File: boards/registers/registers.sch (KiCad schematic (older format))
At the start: 0 parts

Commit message: General-purpose register
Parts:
- added D? (x8): LED, symbol Device:LED
- added R? (x8): LED, symbol Device:R
- added R? (x8): 10k, symbol Device:R
- added U?: 74AC273, symbol 74xx:74HCT273
- added U?: 74ACT244, symbol 74xx:74HC244
- added U? (x3): 74LS08, symbol 74xx:74LS08
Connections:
- net labels added: GND, VCC, a[0..15], a_we, alu_a[0..7], alu_b0, alu_b1, alu_b2, alu_b3, alu_b4, alu_b5, alu_b6, alu_b7, alu_b[0..7], b_we, clk, d0, d1, d2, d3, d4, d5, d6, d7, d[0..7], di0, di1, di2, di3, di4, di5, di6, di7, di[0..7], ir_out0, ir_out1, ir_out2, ir_out3, ir_out4, ir_out5, ir_out6, ir_out7, ir_out[0..7], ir_we, oe_a_d, oe_b_alu, oe_b_d, ~clk, ~d_to_di_oe, ~rst
- wire segments 0 -> 76
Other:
- note added: "5 mA each"
- note added: "IR"
- note added: "TODO\nremove extra chip"

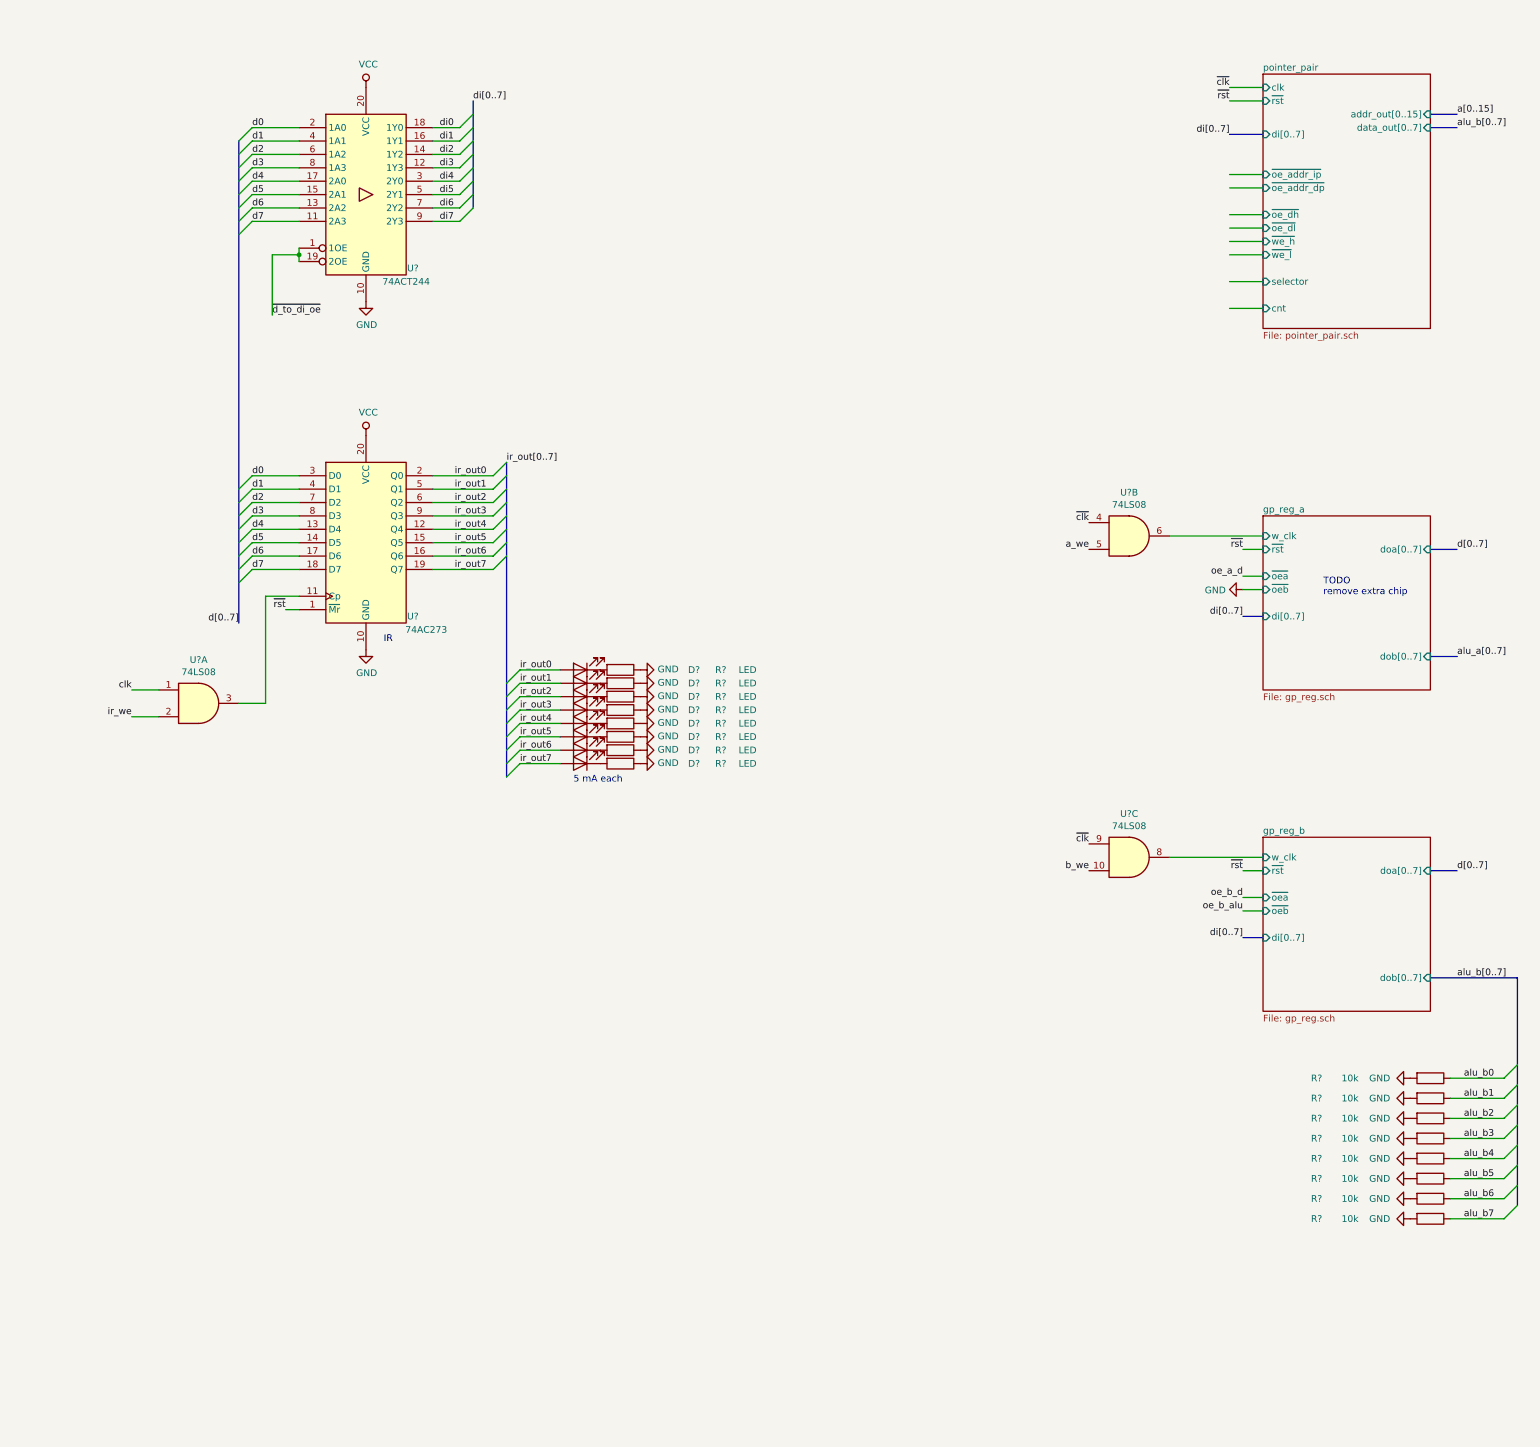
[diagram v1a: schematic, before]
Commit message: Rename some signals in CPU, add capacitors and signal names to the schematics
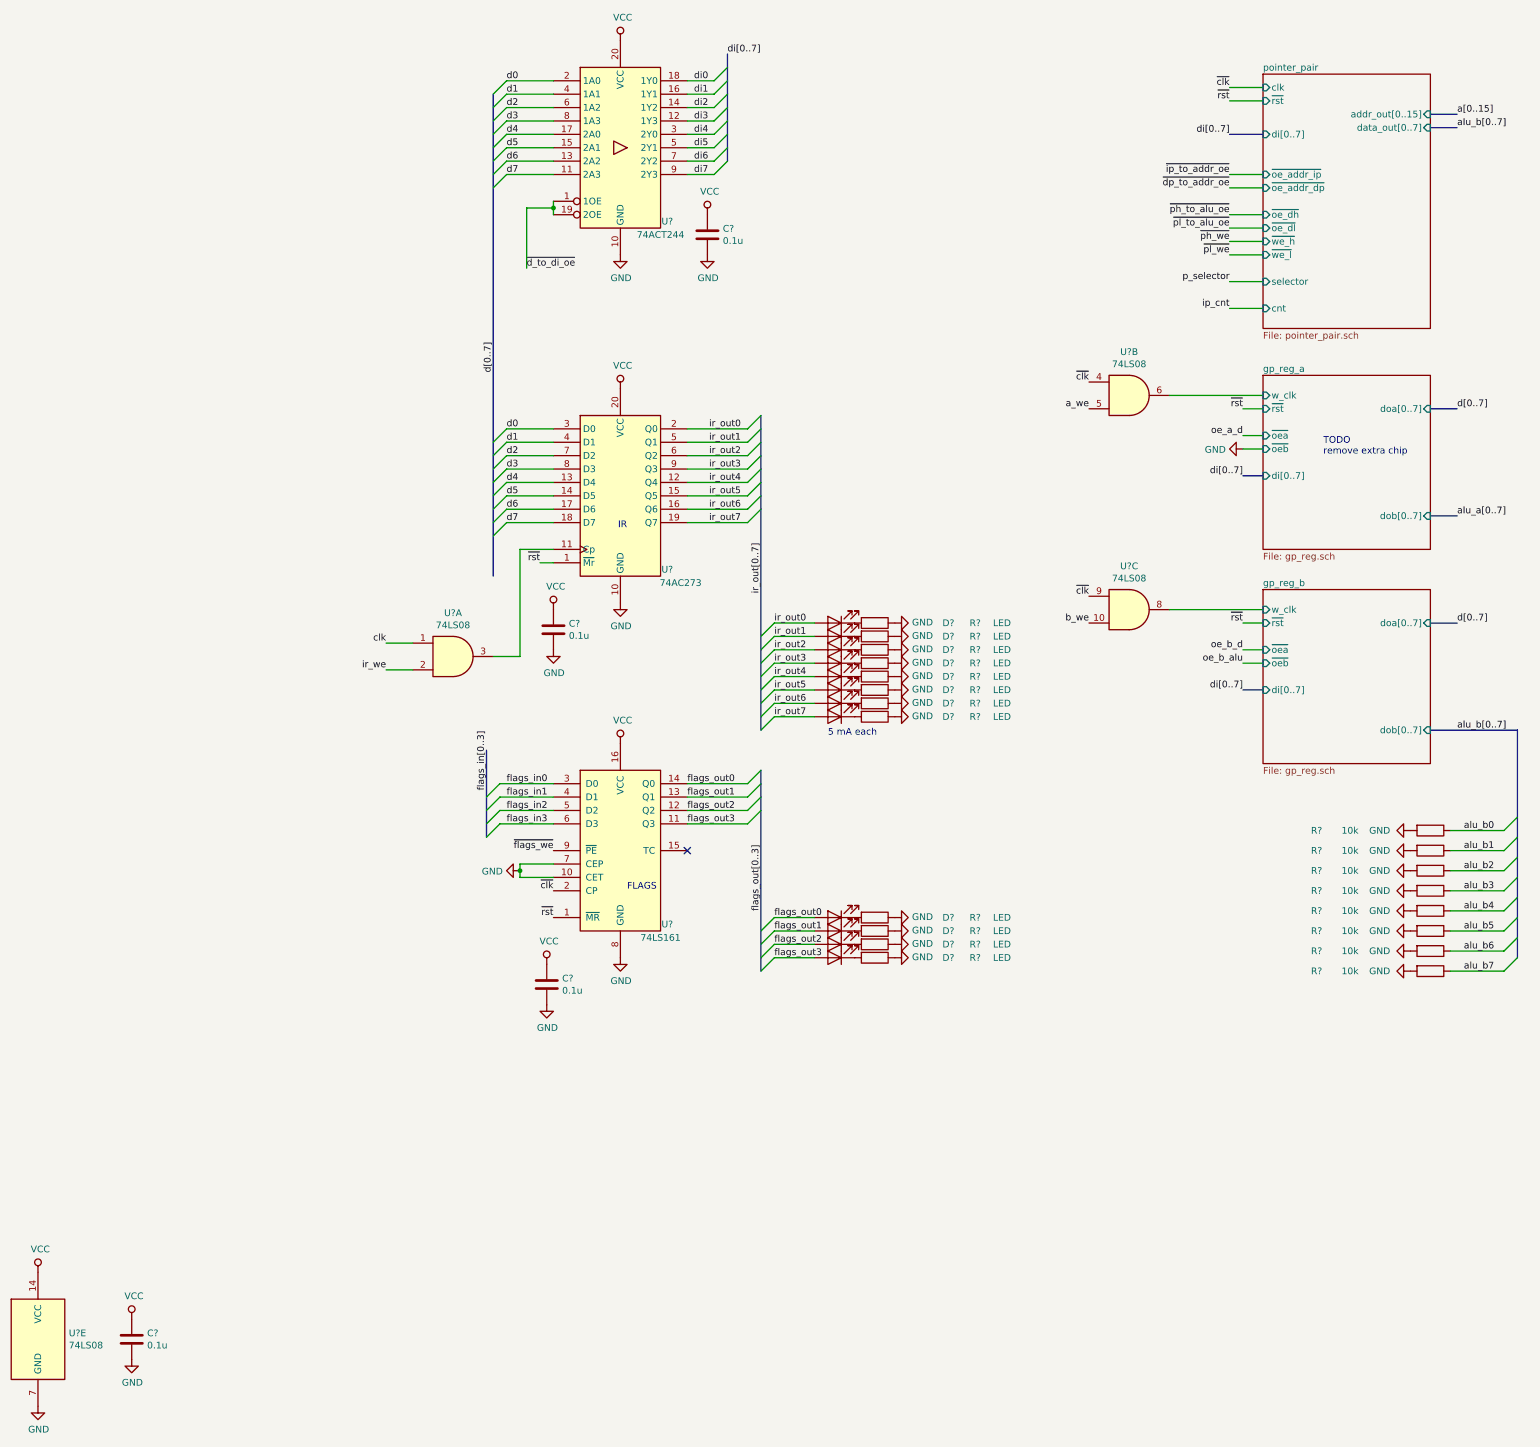
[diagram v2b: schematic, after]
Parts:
- added C? (x4): 0.1u, symbol Device:C
- added D? (x4): LED, symbol Device:LED
- added R? (x4): LED, symbol Device:R
- added U?: 74LS161, symbol 74xx:74LS161
- added U?: 74LS08, symbol 74xx:74LS08
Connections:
- net labels added: flags_in0, flags_in1, flags_in2, flags_in3, flags_in[0..3], flags_out0, flags_out1, flags_out2, flags_out3, flags_out[0..3], ip_cnt, p_selector, ~dp_to_addr_oe, ~flags_we, ~ip_to_addr_oe, ~ph_to_alu_oe, ~ph_we, ~pl_to_alu_oe, ~pl_we
- wire segments 76 -> 92
- no-connect marks 0 -> 1
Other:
- note added: "FLAGS"
- moved on the sheet: D?, R?, U?, U?A, U?B, U?C

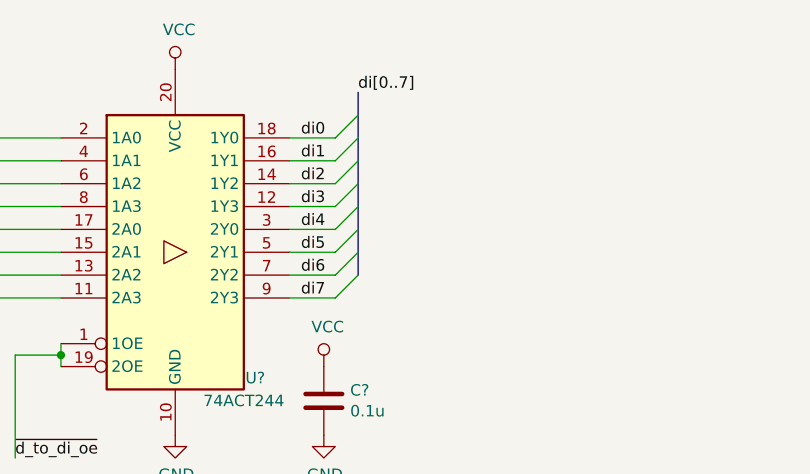
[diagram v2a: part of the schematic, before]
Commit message: Add bus resistors
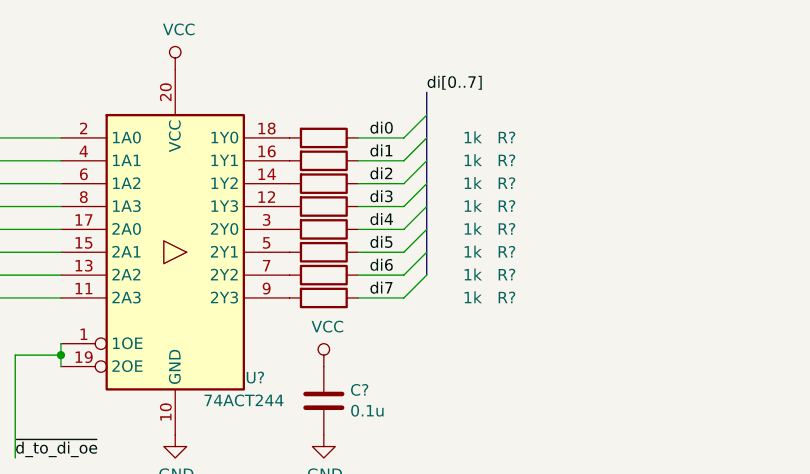
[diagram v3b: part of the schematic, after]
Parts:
- added R? (x8): 1k, symbol Device:R
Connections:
- net di0: now also R?.1; no longer U?.18 (1Y0)
- net di1: now also R?.1; no longer U?.16 (1Y1)
- net di2: now also R?.1; no longer U?.14 (1Y2)
- net di3: now also R?.1; no longer U?.12 (1Y3)
- net di4: now also R?.1; no longer U?.3 (2Y0)
- net di5: now also R?.1; no longer U?.5 (2Y1)
- net di6: now also R?.1; no longer U?.7 (2Y2)
- net di7: now also R?.1; no longer U?.9 (2Y3)
- new net: R?.2, U?.12 (1Y3)
- new net: R?.2, U?.14 (1Y2)
- new net: R?.2, U?.16 (1Y1)
- new net: R?.2, U?.18 (1Y0)
- new net: R?.2, U?.3 (2Y0)
- new net: R?.2, U?.5 (2Y1)
- new net: R?.2, U?.7 (2Y2)
- new net: R?.2, U?.9 (2Y3)
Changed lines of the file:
@@
 d7
 Entry Wire Line
-	6050 1100 6150 1000
-Entry Wire Line
-	6050 1200 6150 1100
-Entry Wire Line
-	6050 1300 6150 1200
-Entry Wire Line
-	6050 1400 6150 1300
-Entry Wire Line
-	6050 1500 6150 1400
-Entry Wire Line
-	6050 1600 6150 1500
-Entry Wire Line
-	6050 1700 6150 1600
-Entry Wire Line
-	6050 1800 6150 1700
-Wire Wire Line
-	6050 1800 5850 1800
-Wire Wire Line
-	5850 1700 6050 1700
-Wire Wire Line
-	6050 1600 5850 1600
-Wire Wire Line
-	5850 1500 6050 1500
-Wire Wire Line
-	6050 1400 5850 1400
-Wire Wire Line
-	5850 1300 6050 1300
-Wire Wire Line
-	6050 1200 5850 1200
-Wire Wire Line
-	5850 1100 6050 1100
-Text Label 6150 900  0    50   ~ 0
+	6350 1100 6450 1000
+Entry Wire Line
+	6350 1200 6450 1100
+Entry Wire Line
+	6350 1300 6450 1200
+Entry Wire Line
+	6350 1400 6450 1300
+Entry Wire Line
+	6350 1500 6450 1400
+Entry Wire Line
+	6350 1600 6450 1500
+Entry Wire Line
+	6350 1700 6450 1600
+Entry Wire Line
+	6350 1800 6450 1700
+Wire Wire Line
+	6350 1800 6150 1800
+Wire Wire Line
+	6150 1700 6350 1700
+Wire Wire Line
+	6350 1600 6150 1600
+Wire Wire Line
+	6150 1500 6350 1500
+Wire Wire Line
+	6350 1400 6150 1400
+Wire Wire Line
+	6150 1300 6350 1300
+Wire Wire Line
+	6350 1200 6150 1200
+Wire Wire Line
+	6150 1100 6350 1100
+Text Label 6450 900  0    50   ~ 0
 di[0..7]
-Text Label 5900 1100 0    50   ~ 0
+Text Label 6200 1100 0    50   ~ 0
 di0
-Text Label 5900 1200 0    50   ~ 0
+Text Label 6200 1200 0    50   ~ 0
 di1
-Text Label 5900 1300 0    50   ~ 0
+Text Label 6200 1300 0    50   ~ 0
 di2
-Text Label 5900 1400 0    50   ~ 0
+Text Label 6200 1400 0    50   ~ 0
 di3
-Text Label 5900 1500 0    50   ~ 0
+Text Label 6200 1500 0    50   ~ 0
 di4
-Text Label 5900 1600 0    50   ~ 0
+Text Label 6200 1600 0    50   ~ 0
 di5
-Text Label 5900 1700 0    50   ~ 0
+Text Label 6200 1700 0    50   ~ 0
 di6
-Text Label 5900 1800 0    50   ~ 0
+Text Label 6200 1800 0    50   ~ 0
 di7
 Wire Wire Line
@@
 	1    0    0    -1
 $EndComp
+$Comp
+L Device:R R?
+U 1 1 5E9A723F
+P 6000 1100
+F 0 "R?" V 6000 1900 50  0000 C CNN
+F 1 "1k" V 6000 1750 50  0000 C CNN
+F 2 "" V 5930 1100 50  0001 C CNN
+F 3 "~" H 6000 1100 50  0001 C CNN
+	1    6000 1100
+	0    1    1    0
+$EndComp
+$Comp
+L Device:R R?
+U 1 1 5E9A7245
+P 6000 1200
+F 0 "R?" V 6000 2000 50  0000 C CNN
+F 1 "1k" V 6000 1850 50  0000 C CNN
+F 2 "" V 5930 1200 50  0001 C CNN
+F 3 "~" H 6000 1200 50  0001 C CNN
+	1    6000 1200
+	0    1    1    0
+$EndComp
+$Comp
+L Device:R R?
+U 1 1 5E9A724B
+P 6000 1300
+F 0 "R?" V 6000 2100 50  0000 C CNN
+F 1 "1k" V 6000 1950 50  0000 C CNN
+F 2 "" V 5930 1300 50  0001 C CNN
+F 3 "~" H 6000 1300 50  0001 C CNN
+	1    6000 1300
+	0    1    1    0
+$EndComp
+$Comp
+L Device:R R?
+U 1 1 5E9A7251
+P 6000 1400
+F 0 "R?" V 6000 2200 50  0000 C CNN
+F 1 "1k" V 6000 2050 50  0000 C CNN
+F 2 "" V 5930 1400 50  0001 C CNN
+F 3 "~" H 6000 1400 50  0001 C CNN
+	1    6000 1400
+	0    1    1    0
+$EndComp
+$Comp
+L Device:R R?
+U 1 1 5E9A7257
+P 6000 1500
+F 0 "R?" V 6000 2300 50  0000 C CNN
+F 1 "1k" V 6000 2150 50  0000 C CNN
+F 2 "" V 5930 1500 50  0001 C CNN
+F 3 "~" H 6000 1500 50  0001 C CNN
+	1    6000 1500
+	0    1    1    0
+$EndComp
+$Comp
+L Device:R R?
+U 1 1 5E9A725D
+P 6000 1600
+F 0 "R?" V 6000 2400 50  0000 C CNN
+F 1 "1k" V 6000 2250 50  0000 C CNN
+F 2 "" V 5930 1600 50  0001 C CNN
+F 3 "~" H 6000 1600 50  0001 C CNN
+	1    6000 1600
+	0    1    1    0
+$EndComp
+$Comp
+L Device:R R?
+U 1 1 5E9A7263
+P 6000 1700
+F 0 "R?" V 6000 2500 50  0000 C CNN
+F 1 "1k" V 6000 2350 50  0000 C CNN
+F 2 "" V 5930 1700 50  0001 C CNN
+F 3 "~" H 6000 1700 50  0001 C CNN
+	1    6000 1700
+	0    1    1    0
+$EndComp
+$Comp
+L Device:R R?
+U 1 1 5E9A7269
+P 6000 1800
+F 0 "R?" V 6000 2600 50  0000 C CNN
+F 1 "1k" V 6000 2450 50  0000 C CNN
+F 2 "" V 5930 1800 50  0001 C CNN
+F 3 "~" H 6000 1800 50  0001 C CNN
+	1    6000 1800
+	0    1    1    0
+$EndComp
 Wire Bus Line
 	4350 6100 4350 6750
@@
 	6400 6250 6400 7750
 Wire Bus Line
-	6150 900  6150 1700
+	6450 900  6450 1700
 Wire Bus Line
 	12050 5950 12050 7650
